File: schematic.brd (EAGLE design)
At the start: 160 x 100 mm, 56 parts, among them J1 FTDI_DEVICERA_SMT, M1 WIRELESS-NRF24L01, Q1 8MHz, T1 NMOS, T2 NMOS, T3 NMOS, T4 NMOS, U1 ATMEGA328P_TQFP, U2 GY-521MPU6050, U3 LTC3534

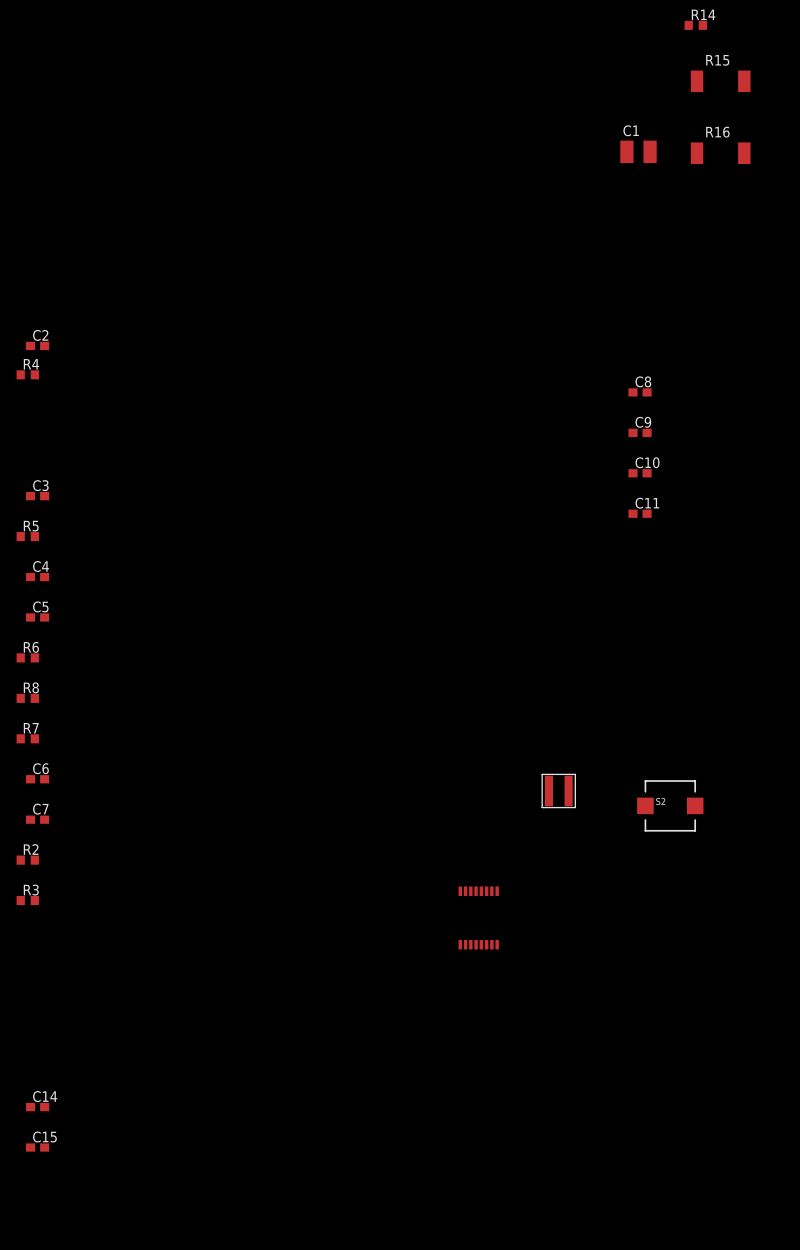
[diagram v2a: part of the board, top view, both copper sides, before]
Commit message: Fixed issues from schematic pre-check
Changed package of R15,R16 to 0603.
CHange 100pF capacitor to 68pF to be closer to recommended value.
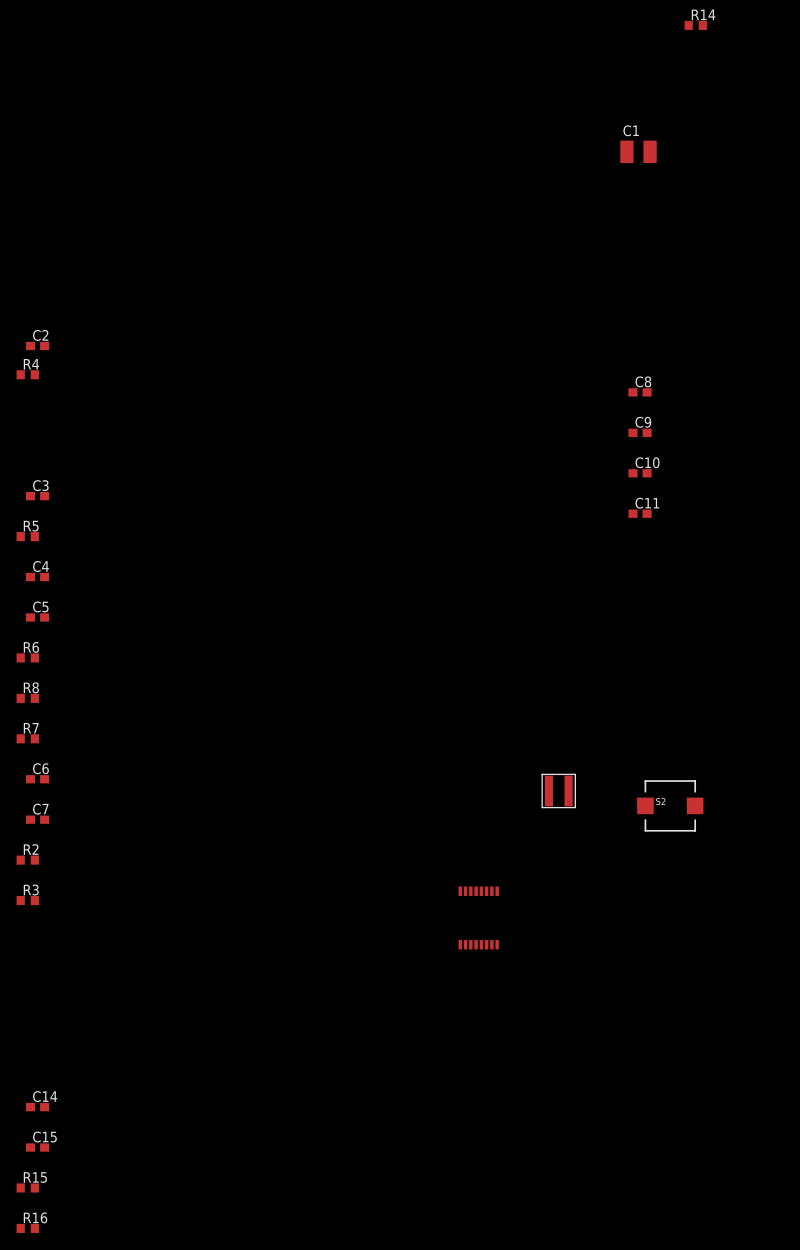
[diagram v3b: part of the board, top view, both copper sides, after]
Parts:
- C4: value 100pF -> 68pF
- R15, R16: device resistor:M2309 -> resistor:R0603
- moved R15 157.4 mm to (-255.9, -27.7)
- moved R16 154.2 mm to (-255.9, -32.6)
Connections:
- net GND: now also R15.1, R16.1; no longer R15.2, R16.2
- net PWM3: now also R15.2; no longer R15.1
- net PWM4: now also R16.2; no longer R16.1
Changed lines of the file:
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@@
 <element name="R13" library="resistor" library_urn="urn:adsk.eagle:library:348" package="R0603" package3d_urn="urn:adsk.eagle:package:26057/1" value="10K" x="-175.351490625" y="117.31990625"/>
 <element name="R14" library="resistor" library_urn="urn:adsk.eagle:library:348" package="R0603" package3d_urn="urn:adsk.eagle:package:26057/1" value="10K" x="-175.351490625" y="112.44310625"/>
-<element name="R15" library="resistor" library_urn="urn:adsk.eagle:library:348" package="M2309" package3d_urn="urn:adsk.eagle:package:26085/1" value="10K" x="-172.351496875" y="105.696765625"/>
-<element name="R16" library="resistor" library_urn="urn:adsk.eagle:library:348" package="M2309" package3d_urn="urn:adsk.eagle:package:26085/1" value="10K" x="-172.351496875" y="97.03010625"/>
 <element name="C1" library="rcl" library_urn="urn:adsk.eagle:library:334" package="C1210" package3d_urn="urn:adsk.eagle:package:23619/2" value="100uF" x="-182.259021875" y="97.19678125">
 <attribute name="SPICEPREFIX" value="C" x="-182.259021875" y="97.19678125" size="0.1" layer="27" display="off"/>
@@
 <element name="C3" library="resistor" library_urn="urn:adsk.eagle:library:348" package="C0603" package3d_urn="urn:adsk.eagle:package:26138/1" value="10uF" x="-254.7182625" y="55.675603125"/>
 <element name="R5" library="resistor" library_urn="urn:adsk.eagle:library:348" package="R0603" package3d_urn="urn:adsk.eagle:package:26057/1" value="10K" x="-255.903175" y="50.798803125"/>
-<element name="C4" library="resistor" library_urn="urn:adsk.eagle:library:348" package="C0603" package3d_urn="urn:adsk.eagle:package:26138/1" value="100pF" x="-254.7182625" y="45.922003125"/>
+<element name="C4" library="resistor" library_urn="urn:adsk.eagle:library:348" package="C0603" package3d_urn="urn:adsk.eagle:package:26138/1" value="68pF" x="-254.7182625" y="45.922003125"/>
 <element name="C5" library="resistor" library_urn="urn:adsk.eagle:library:348" package="C0603" package3d_urn="urn:adsk.eagle:package:26138/1" value="22uF" x="-254.7182625" y="41.045203125"/>
 <element name="R6" library="resistor" library_urn="urn:adsk.eagle:library:348" package="R0603" package3d_urn="urn:adsk.eagle:package:26057/1" value="374K" x="-255.903175" y="36.168403125"/>
@@
 <element name="C14" library="resistor" library_urn="urn:adsk.eagle:library:348" package="C0603" package3d_urn="urn:adsk.eagle:package:26138/1" value="10uF" x="-254.7182625" y="-17.99544375"/>
 <element name="C15" library="resistor" library_urn="urn:adsk.eagle:library:348" package="C0603" package3d_urn="urn:adsk.eagle:package:26138/1" value="0.1uF" x="-254.7182625" y="-22.87224375"/>
+<element name="R15" library="resistor" library_urn="urn:adsk.eagle:library:348" package="R0603" package3d_urn="urn:adsk.eagle:package:26057/1" value="10K" x="-255.903171875" y="-27.74904375"/>
+<element name="R16" library="resistor" library_urn="urn:adsk.eagle:library:348" package="R0603" package3d_urn="urn:adsk.eagle:package:26057/1" value="10K" x="-255.903171875" y="-32.62584375"/>
 </elements>
 <signals>
@@
 <contactref element="R13" pad="1"/>
 <contactref element="R14" pad="1"/>
-<contactref element="R15" pad="2"/>
-<contactref element="R16" pad="2"/>
 <contactref element="C1" pad="2"/>
 <contactref element="C9" pad="2"/>
@@
 <contactref element="C14" pad="2"/>
 <contactref element="C15" pad="2"/>
+<contactref element="R15" pad="1"/>
+<contactref element="R16" pad="1"/>
 <wire x1="-256.753175" y1="31.291603125" x2="-256.753175" y2="6.907603125" width="0" layer="19" extent="1-1"/>
 <wire x1="-253.8682625" y1="41.045203125" x2="-256.753175" y2="31.291603125" width="0" layer="19" extent="1-1"/>
@@
 <wire x1="-253.8682625" y1="-17.99544375" x2="-256.753175" y2="6.907603125" width="0" layer="19" extent="1-1"/>
 <wire x1="-253.8682625" y1="-22.87224375" x2="-253.8682625" y2="-17.99544375" width="0" layer="19" extent="1-1"/>
+<wire x1="-256.753171875" y1="-27.74904375" x2="-253.8682625" y2="-22.87224375" width="0" layer="19" extent="1-1"/>
+<wire x1="-256.753171875" y1="-32.62584375" x2="-256.753171875" y2="-27.74904375" width="0" layer="19" extent="1-1"/>
 <wire x1="-203.748209375" y1="8.034984375" x2="-256.753175" y2="6.907603125" width="0" layer="19" extent="1-1"/>
 <wire x1="-199.303209375" y1="8.034984375" x2="-203.748209375" y2="8.034984375" width="0" layer="19" extent="1-1"/>
@@
 <wire x1="-181.224084375" y1="63.308965625" x2="-181.224084375" y2="58.432165625" width="0" layer="19" extent="1-1"/>
 <wire x1="-180.859021875" y1="97.19678125" x2="-181.224084375" y2="63.308965625" width="0" layer="19" extent="1-1"/>
-<wire x1="-169.501496875" y1="97.03010625" x2="-180.859021875" y2="97.19678125" width="0" layer="19" extent="1-1"/>
-<wire x1="-169.501496875" y1="105.696765625" x2="-169.501496875" y2="97.03010625" width="0" layer="19" extent="1-1"/>
-<wire x1="-176.201490625" y1="112.44310625" x2="-169.501496875" y2="105.696765625" width="0" layer="19" extent="1-1"/>
+<wire x1="-176.201490625" y1="112.44310625" x2="-180.859021875" y2="97.19678125" width="0" layer="19" extent="1-1"/>
 <wire x1="-176.201490625" y1="117.31990625" x2="-176.201490625" y2="112.44310625" width="0" layer="19" extent="1-1"/>
 <wire x1="-175.51658125" y1="127.168528125" x2="-176.201490625" y2="117.31990625" width="0" layer="19" extent="1-1"/>
@@
 <contactref element="T3" pad="1"/>
 <contactref element="U1" pad="10"/>
-<contactref element="R15" pad="1"/>
-<wire x1="-64.45" y1="67.58" x2="-175.201496875" y2="105.696765625" width="0" layer="19" extent="1-1"/>
+<contactref element="R15" pad="2"/>
+<wire x1="-64.45" y1="67.58" x2="-255.053171875" y2="-27.74904375" width="0" layer="19" extent="1-1"/>
 <wire x1="-40.1" y1="24.9174" x2="-64.45" y2="67.58" width="0" layer="19" extent="1-1"/>
 </signal>
@@
 <contactref element="U1" pad="13"/>
 <contactref element="T4" pad="1"/>
-<contactref element="R16" pad="1"/>
-<wire x1="-25.08" y1="72.66" x2="-175.201496875" y2="97.03010625" width="0" layer="19" extent="1-1"/>
+<contactref element="R16" pad="2"/>
 <wire x1="-37.7" y1="24.9174" x2="-25.08" y2="72.66" width="0" layer="19" extent="1-1"/>
+<wire x1="-255.053171875" y1="-32.62584375" x2="-37.7" y2="24.9174" width="0" layer="19" extent="1-1"/>
 </signal>
 <signal name="N$10">

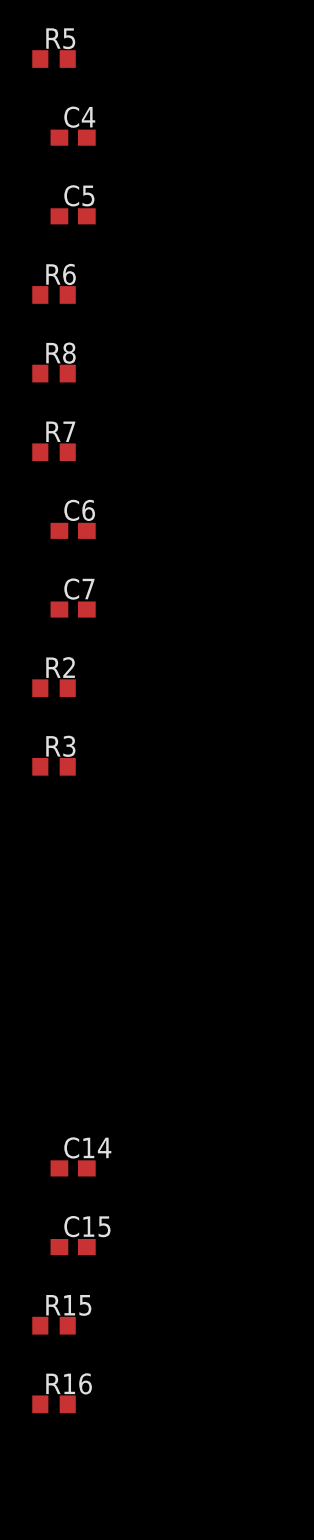
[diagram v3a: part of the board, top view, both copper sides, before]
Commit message: 65pF capacitor 1206 package
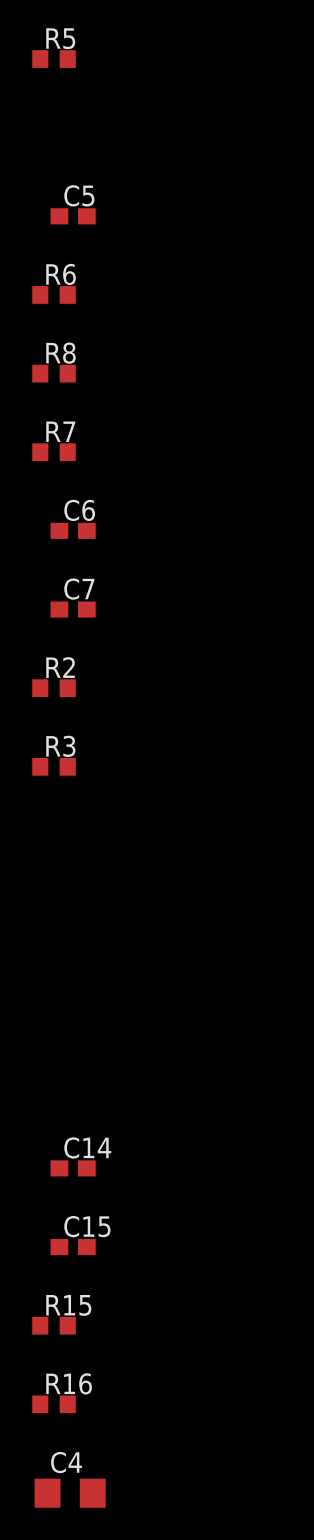
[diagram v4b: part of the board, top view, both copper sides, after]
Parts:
- C4: value 68pF -> 65pF; device resistor:C0603 -> rcl:C1206
- moved C4 84.1 mm to (-254.9, -38.1)
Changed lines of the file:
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@@
 <element name="C3" library="resistor" library_urn="urn:adsk.eagle:library:348" package="C0603" package3d_urn="urn:adsk.eagle:package:26138/1" value="10uF" x="-254.7182625" y="55.675603125"/>
 <element name="R5" library="resistor" library_urn="urn:adsk.eagle:library:348" package="R0603" package3d_urn="urn:adsk.eagle:package:26057/1" value="10K" x="-255.903175" y="50.798803125"/>
-<element name="C4" library="resistor" library_urn="urn:adsk.eagle:library:348" package="C0603" package3d_urn="urn:adsk.eagle:package:26138/1" value="68pF" x="-254.7182625" y="45.922003125"/>
 <element name="C5" library="resistor" library_urn="urn:adsk.eagle:library:348" package="C0603" package3d_urn="urn:adsk.eagle:package:26138/1" value="22uF" x="-254.7182625" y="41.045203125"/>
 <element name="R6" library="resistor" library_urn="urn:adsk.eagle:library:348" package="R0603" package3d_urn="urn:adsk.eagle:package:26057/1" value="374K" x="-255.903175" y="36.168403125"/>
@@
 <element name="R15" library="resistor" library_urn="urn:adsk.eagle:library:348" package="R0603" package3d_urn="urn:adsk.eagle:package:26057/1" value="10K" x="-255.903171875" y="-27.74904375"/>
 <element name="R16" library="resistor" library_urn="urn:adsk.eagle:library:348" package="R0603" package3d_urn="urn:adsk.eagle:package:26057/1" value="10K" x="-255.903171875" y="-32.62584375"/>
+<element name="C4" library="rcl" library_urn="urn:adsk.eagle:library:334" package="C1206" package3d_urn="urn:adsk.eagle:package:23618/2" value="65pF" x="-254.903171875" y="-38.13764375">
+<attribute name="SPICEPREFIX" value="C" x="-254.903171875" y="-38.13764375" size="1.778" layer="27" display="off"/>
+</element>
 </elements>
 <signals>
@@
 <signal name="N$18">
 <contactref element="U3" pad="15"/>
-<contactref element="C4" pad="2"/>
 <contactref element="R6" pad="1"/>
 <contactref element="R8" pad="2"/>
 <contactref element="R7" pad="1"/>
 <contactref element="C7" pad="2"/>
+<contactref element="C4" pad="2"/>
 <wire x1="-256.753175" y1="26.414803125" x2="-253.8682625" y2="16.661203125" width="0" layer="19" extent="1-1"/>
 <wire x1="-255.053175" y1="31.291603125" x2="-256.753175" y2="26.414803125" width="0" layer="19" extent="1-1"/>
 <wire x1="-256.753175" y1="36.168403125" x2="-255.053175" y2="31.291603125" width="0" layer="19" extent="1-1"/>
-<wire x1="-253.8682625" y1="45.922003125" x2="-256.753175" y2="36.168403125" width="0" layer="19" extent="1-1"/>
 <wire x1="-203.113209375" y1="8.034984375" x2="-253.8682625" y2="16.661203125" width="0" layer="19" extent="1-1"/>
+<wire x1="-253.503171875" y1="-38.13764375" x2="-253.8682625" y2="16.661203125" width="0" layer="19" extent="1-1"/>
 </signal>
 <signal name="N$20">
@@
 <wire x1="-202.478209375" y1="8.034984375" x2="-255.5682625" y2="16.661203125" width="0" layer="19" extent="1-1"/>
 </signal>
-<signal name="N$15">
+<signal name="N$14">
 <contactref element="R5" pad="1"/>
 <contactref element="C4" pad="1"/>
-<wire x1="-255.5682625" y1="45.922003125" x2="-256.753175" y2="50.798803125" width="0" layer="19" extent="1-1"/>
+<wire x1="-256.303171875" y1="-38.13764375" x2="-256.753175" y2="50.798803125" width="0" layer="19" extent="1-1"/>
 </signal>
 </signals>

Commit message: fixed programmer RX TX
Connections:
- net RXD: now also J1.3; no longer J1.2
- net TXD: now also J1.2; no longer J1.3
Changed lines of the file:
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@@
 </signal>
 <signal name="TXD">
-<contactref element="J1" pad="3"/>
 <contactref element="U1" pad="31"/>
-<wire x1="-40.1" y1="33.5026" x2="-25.4" y2="35.48" width="0" layer="19" extent="1-1"/>
+<contactref element="J1" pad="2"/>
+<wire x1="-27.94" y1="35.48" x2="-40.1" y2="33.5026" width="0" layer="19" extent="1-1"/>
 </signal>
 <signal name="RXD">
-<contactref element="J1" pad="2"/>
 <contactref element="U1" pad="30"/>
-<wire x1="-39.3" y1="33.5026" x2="-27.94" y2="35.48" width="0" layer="19" extent="1-1"/>
+<contactref element="J1" pad="3"/>
+<wire x1="-39.3" y1="33.5026" x2="-25.4" y2="35.48" width="0" layer="19" extent="1-1"/>
 </signal>
 <signal name="CE">
